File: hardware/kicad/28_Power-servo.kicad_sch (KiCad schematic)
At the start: 18 parts, among them U55 TPSM63610RDFR

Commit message: servo buck done
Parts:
- removed C67: 22pF, Capacitor_SMD:C_0402_1005Metric, symbol 5v rail sm-easyedapro:C0402C220K5RACAUTO
- removed JP2: Jumper_2_Bridged, Jumper:SolderJumper-2_P1.3mm_Bridged_RoundedPad1.0x1.5mm, symbol Jumper:Jumper_2_Bridged
- removed NT17: NetTie_2, NetTie:NetTie-2_SMD_Pad2.0mm, symbol Device:NetTie_2
- removed R118: 100kΩ, Resistor_SMD:R_0402_1005Metric, symbol 5v rail sm-easyedapro:FRC0402F1003TS
- added C1701: 100nF, Capacitor_SMD:C_0603_1608Metric, symbol Device:C
- added JP1701: Jumper_2_Small_Bridged, PCM_SparkFun-Jumper:Jumper_2_NC_Trace, symbol Jumper:Jumper_2_Small_Bridged
- added NT1702: NetTie_2, 5v rail sm-easyedapro:NetTie-2_SMD_Pad0.2mm, symbol Device:NetTie_2
- R117: footprint Resistor_SMD:R_0603_1608Metric -> Resistor_SMD:R_0402_1005Metric; LCSC Part Name 26.7kΩ ±1% 100mW 厚膜电阻 -> (none); Manufacturer UNI-ROYAL(厚声) -> (none); Manufacturer Part 0603WAF2672T5E -> (none); Supplier LCSC -> (none); Supplier Part C22923 -> (none)
- R120: footprint Resistor_SMD:R_0603_1608Metric -> Resistor_SMD:R_0402_1005Metric; LCSC Part Name 47kΩ ±1% 100mW 厚膜电阻 -> (none); Manufacturer UNI-ROYAL(厚声) -> (none); Manufacturer Part 0603WAF4702T5E -> (none); Supplier LCSC -> (none); Supplier Part C25819 -> (none)
- R121: now not fitted; now left out of the parts list
- R122: LCSC Part Name 100kΩ ±1% 62.5mW 厚膜电阻 -> (none); Manufacturer FOJAN(富捷) -> (none); Manufacturer Part FRC0402F1003TS -> (none); Supplier LCSC -> (none); Supplier Part C2906859 -> (none)
- R123: footprint Resistor_SMD:R_0603_1608Metric -> Resistor_SMD:R_0402_1005Metric; LCSC Part Name 20kΩ ±1% 100mW 厚膜电阻 -> (none); Manufacturer UNI-ROYAL(厚声) -> (none); Manufacturer Part 0603WAF2002T5E -> (none); Supplier LCSC -> (none); Supplier Part C4184 -> (none)
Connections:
- net GNDA: now also C65.1, C66.2, C68.2, C69.1, C70.1, C71.1, U55.19 (PGND), U55.20 (PGND), C1701.1, JP1701.2 (B), NT1702.1
- net OUT: now also C1701.2
- net at U55.14 (SPSP): now also JP1701.1 (A)
- net at U55.15 (MODE): now also NT1702.2
- removed net GND: C65.1, C66.2, C68.2, C69.1, C70.1, C71.1, U55.16 (NC), U55.19 (PGND), U55.20 (PGND)
- no-connect marks 2 -> 3
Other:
- note added: "highest efficiency, bad emi default cut trace an place 100 ohm for better balance"
- note removed: "highest efficiency, bad emi default cut trace for 100 ohm for better balance"

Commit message: starting erc check
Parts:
- C65, C66, C69, C70, C71: footprint Capacitor_SMD:C_1210_3225Metric -> 5v rail sm-easyedapro:C1210
- R117: footprint Resistor_SMD:R_0402_1005Metric -> 5v rail sm-easyedapro:R0603; LCSC Part Name (none) -> 26.7kΩ ±1% 100mW 厚膜电阻; Manufacturer (none) -> UNI-ROYAL(厚声); Manufacturer Part (none) -> 0603WAF2672T5E; Supplier (none) -> LCSC; Supplier Part (none) -> C22923
- R119: footprint Resistor_SMD:R_0402_1005Metric -> 5v rail sm-easyedapro:R0402
- R120: footprint Resistor_SMD:R_0402_1005Metric -> 5v rail sm-easyedapro:R0603; LCSC Part Name (none) -> 47kΩ ±1% 100mW 厚膜电阻; Manufacturer (none) -> UNI-ROYAL(厚声); Manufacturer Part (none) -> 0603WAF4702T5E; Supplier (none) -> LCSC; Supplier Part (none) -> C25819
- R121: footprint Resistor_SMD:R_0603_1608Metric -> 5v rail sm-easyedapro:R0603
- R122: footprint Resistor_SMD:R_0402_1005Metric -> 5v rail sm-easyedapro:R0402; LCSC Part Name (none) -> 100kΩ ±1% 62.5mW 厚膜电阻; Manufacturer (none) -> FOJAN(富捷); Manufacturer Part (none) -> FRC0402F1003TS; Supplier (none) -> LCSC; Supplier Part (none) -> C2906859
- R123: footprint Resistor_SMD:R_0402_1005Metric -> 5v rail sm-easyedapro:R0603; LCSC Part Name (none) -> 20kΩ ±1% 100mW 厚膜电阻; Manufacturer (none) -> UNI-ROYAL(厚声); Manufacturer Part (none) -> 0603WAF2002T5E; Supplier (none) -> LCSC; Supplier Part (none) -> C4184
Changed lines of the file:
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@@
 			)
 		)
-		(property "Footprint" "Capacitor_SMD:C_1210_3225Metric"
+		(property "Footprint" "5v rail sm-easyedapro:C1210"
 			(at 307.34 92.71 0)
 			(effects
@@
 			)
 		)
-		(property "Footprint" "Resistor_SMD:R_0402_1005Metric"
+		(property "Footprint" "5v rail sm-easyedapro:R0603"
 			(at 279.4 111.76 0)
 			(effects
@@
 			)
 		)
-		(property "Datasheet" ""
+		(property "Datasheet" "https://item.szlcsc.com/datasheet/0603WAF2002T5E/4591.html"
 			(at 279.4 111.76 0)
 			(effects
@@
 			)
 		)
-		(property "Description" ""
+		(property "Description" "Type:Thick Film Resistor Resistance:20kΩ Tolerance:±1% Tolerance:±1% Power(Watts):100mW Voltage-Supply(Max):75V Temperature Coefficient:±100ppm/°C Temperature Coefficient:±100ppm/°C Operating Temperature:-55°C~+155°C Operating Temperature:-55°C~+155°C"
 			(at 279.4 111.76 0)
 			(effects
@@
 			)
 		)
-		(property "Manufacturer Part" ""
+		(property "Manufacturer Part" "0603WAF2002T5E"
 			(at 279.4 111.76 0)
 			(effects
@@
 			)
 		)
-		(property "Manufacturer" ""
+		(property "Manufacturer" "UNI-ROYAL(厚声)"
 			(at 279.4 111.76 0)
 			(effects
@@
 			)
 		)
-		(property "Supplier Part" ""
+		(property "Supplier Part" "C4184"
 			(at 279.4 111.76 0)
 			(effects
@@
 			)
 		)
-		(property "Supplier" ""
+		(property "Supplier" "LCSC"
 			(at 279.4 111.76 0)
 			(effects
@@
 			)
 		)
-		(property "LCSC Part Name" ""
+		(property "LCSC Part Name" "20kΩ ±1% 100mW 厚膜电阻"
 			(at 279.4 111.76 0)
 			(effects
@@
 			)
 		)
-		(property "Footprint" "Capacitor_SMD:C_1210_3225Metric"
+		(property "Footprint" "5v rail sm-easyedapro:C1210"
 			(at 139.7 125.73 0)
 			(effects
@@
 			)
 		)
-		(property "Footprint" "Capacitor_SMD:C_1210_3225Metric"
+		(property "Footprint" "5v rail sm-easyedapro:C1210"
 			(at 334.01 92.71 0)
 			(effects
@@
 			)
 		)
-		(property "Datasheet" ""
+		(property "Datasheet" "~"
 			(at 220.98 107.95 0)
 			(effects
@@
 			)
 		)
-		(property "Description" ""
+		(property "Description" "Jumper, 2-pole, closed/bridged"
 			(at 220.98 107.95 0)
 			(effects
@@
 			)
 		)
-		(property "Description" ""
+		(property "Description" "Power symbol creates a global label with name \"GNDA\" , analog ground"
 			(at 243.84 144.78 0)
 			(effects
@@
 			)
 		)
-		(property "Footprint" "Capacitor_SMD:C_1210_3225Metric"
+		(property "Footprint" "5v rail sm-easyedapro:C1210"
 			(at 166.37 125.73 0)
 			(effects
@@
 			)
 		)
-		(property "Footprint" "Resistor_SMD:R_0402_1005Metric"
+		(property "Footprint" "5v rail sm-easyedapro:R0402"
 			(at 279.4 93.98 0)
 			(effects
@@
 			)
 		)
-		(property "Description" ""
+		(property "Description" "Type:Thick Film Resistor Resistance:100kΩ Tolerance:±1% Tolerance:±1% Power(Watts):62.5mW Voltage-Supply(Max):50V Temperature Coefficient:±100ppm/°C Temperature Coefficient:±100ppm/°C Operating Temperature:-55°C~+155°C Operating Temperature:-55°C~+155°C"
 			(at 279.4 93.98 0)
 			(effects
@@
 			)
 		)
-		(property "Manufacturer Part" ""
+		(property "Manufacturer Part" "FRC0402F1003TS"
 			(at 279.4 93.98 0)
 			(effects
@@
 			)
 		)
-		(property "Manufacturer" ""
+		(property "Manufacturer" "FOJAN(富捷)"
 			(at 279.4 93.98 0)
 			(effects
@@
 			)
 		)
-		(property "Supplier Part" ""
+		(property "Supplier Part" "C2906859"
 			(at 279.4 93.98 0)
 			(effects
@@
 			)
 		)
-		(property "Supplier" ""
+		(property "Supplier" "LCSC"
 			(at 279.4 93.98 0)
 			(effects
@@
 			)
 		)
-		(property "LCSC Part Name" ""
+		(property "LCSC Part Name" "100kΩ ±1% 62.5mW 厚膜电阻"
 			(at 279.4 93.98 0)
 			(effects
@@
 			)
 		)
-		(property "Description" ""
+		(property "Description" "Power symbol creates a global label with name \"GNDA\" , analog ground"
 			(at 44.45 132.08 0)
 			(effects
@@
 			)
 		)
-		(property "Description" ""
+		(property "Description" "Power symbol creates a global label with name \"GNDA\" , analog ground"
 			(at 279.4 137.16 0)
 			(effects
@@
 			)
 		)
-		(property "Footprint" "Resistor_SMD:R_0402_1005Metric"
+		(property "Footprint" "5v rail sm-easyedapro:R0603"
 			(at 36.83 119.38 0)
 			(effects
@@
 			)
 		)
-		(property "Datasheet" ""
+		(property "Datasheet" "https://item.szlcsc.com/datasheet/0603WAF2672T5E/23650.html"
 			(at 36.83 119.38 0)
 			(effects
@@
 			)
 		)
-		(property "Description" ""
+		(property "Description" "Type:Thick Film Resistor Resistance:26.7kΩ Tolerance:±1% Tolerance:±1% Power(Watts):100mW Voltage-Supply(Max):75V Temperature Coefficient:±100ppm/°C Temperature Coefficient:±100ppm/°C Operating Temperature:-55°C~+155°C Operating Temperature:-55°C~+155°C"
 			(at 36.83 119.38 0)
 			(effects
@@
 			)
 		)
-		(property "Manufacturer Part" ""
+		(property "Manufacturer Part" "0603WAF2672T5E"
 			(at 36.83 119.38 0)
 			(effects
@@
 			)
 		)
-		(property "Manufacturer" ""
+		(property "Manufacturer" "UNI-ROYAL(厚声)"
 			(at 36.83 119.38 0)
 			(effects
@@
 			)
 		)
-		(property "Supplier Part" ""
+		(property "Supplier Part" "C22923"
 			(at 36.83 119.38 0)
 			(effects
@@
 			)
 		)
-		(property "Supplier" ""
+		(property "Supplier" "LCSC"
 			(at 36.83 119.38 0)
 			(effects
@@
 			)
 		)
-		(property "LCSC Part Name" ""
+		(property "LCSC Part Name" "26.7kΩ ±1% 100mW 厚膜电阻"
 			(at 36.83 119.38 0)
 			(effects
@@
 			)
 		)
-		(property "Footprint" "Resistor_SMD:R_0402_1005Metric"
+		(property "Footprint" "5v rail sm-easyedapro:R0603"
 			(at 157.48 69.85 0)
 			(effects
@@
 			)
 		)
-		(property "Datasheet" ""
+		(property "Datasheet" "https://item.szlcsc.com/datasheet/0603WAF4702T5E/26562.html"
 			(at 157.48 69.85 0)
 			(effects
@@
 			)
 		)
-		(property "Description" ""
+		(property "Description" "Type:Thick Film Resistor Resistance:47kΩ Tolerance:±1% Tolerance:±1% Power(Watts):100mW Voltage-Supply(Max):75V Temperature Coefficient:±100ppm/°C Temperature Coefficient:±100ppm/°C Operating Temperature:-55°C~+155°C Operating Temperature:-55°C~+155°C"
 			(at 157.48 69.85 0)
 			(effects
@@
 			)
 		)
-		(property "Manufacturer Part" ""
+		(property "Manufacturer Part" "0603WAF4702T5E"
 			(at 157.48 69.85 0)
 			(effects
@@
 			)
 		)
-		(property "Manufacturer" ""
+		(property "Manufacturer" "UNI-ROYAL(厚声)"
 			(at 157.48 69.85 0)
 			(effects
@@
 			)
 		)
-		(property "Supplier Part" ""
+		(property "Supplier Part" "C25819"
 			(at 157.48 69.85 0)
 			(effects
@@
 			)
 		)
-		(property "Supplier" ""
+		(property "Supplier" "LCSC"
 			(at 157.48 69.85 0)
 			(effects
@@
 			)
 		)
-		(property "LCSC Part Name" ""
+		(property "LCSC Part Name" "47kΩ ±1% 100mW 厚膜电阻"
 			(at 157.48 69.85 0)
 			(effects
@@
 			)
 		)
-		(property "Description" ""
+		(property "Description" "Power symbol creates a global label with name \"GNDA\" , analog ground"
 			(at 115.57 127 0)
 			(effects
@@
 			)
 		)
-		(property "Footprint" "Resistor_SMD:R_0603_1608Metric"
+		(property "Footprint" "5v rail sm-easyedapro:R0603"
 			(at 234.95 107.95 0)
 			(effects
@@
 			)
 		)
-		(property "Footprint" "Capacitor_SMD:C_1210_3225Metric"
+		(property "Footprint" "5v rail sm-easyedapro:C1210"
 			(at 320.04 92.71 0)
 			(effects
@@
 			)
 		)
-		(property "Description" ""
+		(property "Description" "Power symbol creates a global label with name \"GNDA\" , analog ground"
 			(at 201.93 138.43 0)
 			(effects
@@
 			)
 		)
-		(property "Footprint" "Resistor_SMD:R_0402_1005Metric"
+		(property "Footprint" "5v rail sm-easyedapro:R0402"
 			(at 115.57 110.49 0)
 			(effects
@@
 			)
 		)
-		(property "Description" "Power-5V"
+		(property "Description" "Power symbol creates a global label with name \"+3V3\""
 			(at 157.48 63.5 0)
 			(effects
@@
 			)
 		)
-		(property "Description" ""
+		(property "Description" "Power symbol creates a global label with name \"GNDA\" , analog ground"
 			(at 92.71 128.27 0)
 			(effects

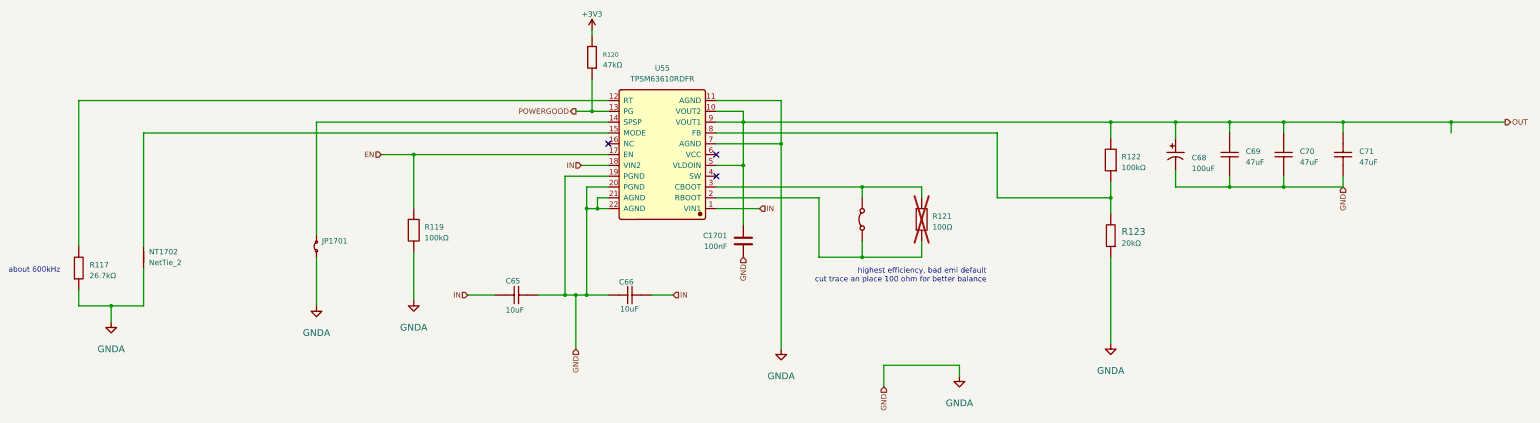
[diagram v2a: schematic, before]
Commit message: fixed some drc issues
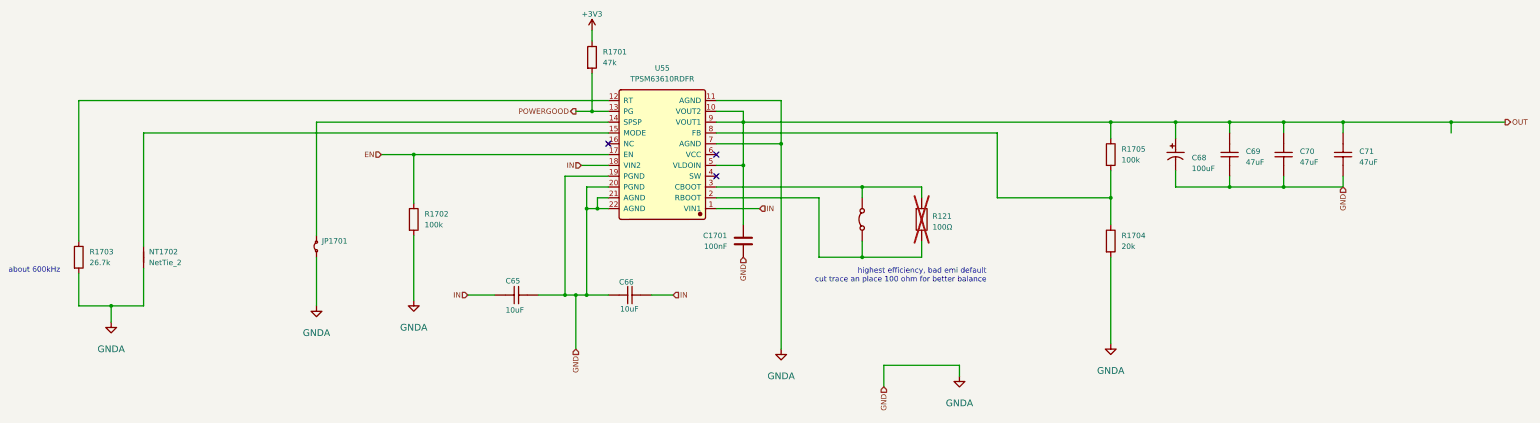
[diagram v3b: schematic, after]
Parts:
- removed R117: 26.7kΩ, 5v rail sm-easyedapro:R0603, symbol 5v rail sm-easyedapro:0603WAF2672T5E
- removed R119, R122: 100kΩ, 5v rail sm-easyedapro:R0402, symbol 5v rail sm-easyedapro:FRC0402F1003TS
- removed R120: 47kΩ, 5v rail sm-easyedapro:R0603, symbol 5v rail sm-easyedapro:0603WAF4702T5E
- removed R123: 20kΩ, 5v rail sm-easyedapro:R0603, symbol 5v rail sm-easyedapro:0603WAF2002T5E
- added R1701: 47k, Resistor_SMD:R_0402_1005Metric, symbol Device:R
- added R1702, R1705: 100k, Resistor_SMD:R_0402_1005Metric, symbol Device:R
- added R1703: 26.7k, Resistor_SMD:R_0402_1005Metric, symbol Device:R
- added R1704: 20k, Resistor_SMD:R_0402_1005Metric, symbol Device:R
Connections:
- net +3V3: now also R1701.1
- net EN: now also R1702.1
- net GNDA: now also R1702.2, R1703.2, R1704.2
- net OUT: now also R1705.1
- net POWERGOOD: now also R1701.2
- net at U55.8 (FB): now also R1704.1, R1705.2
- net at U55.12 (RT): now also R1703.1

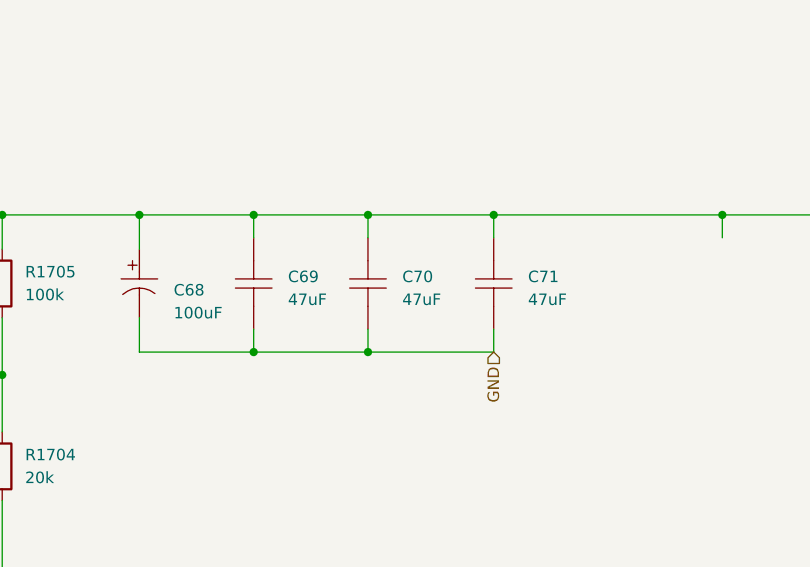
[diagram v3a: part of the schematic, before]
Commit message: about to switch to 3v3 reg instead of buck
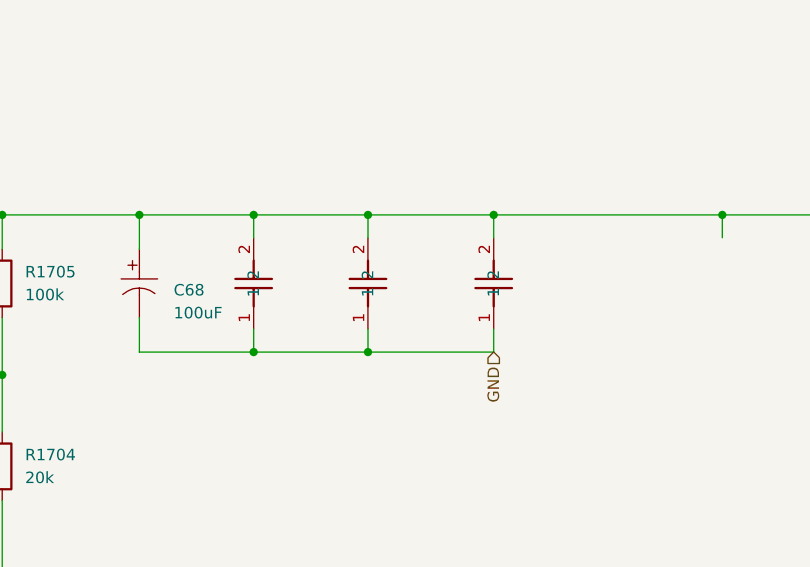
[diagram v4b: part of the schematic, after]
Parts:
- removed C69, C70, C71: 47uF, 5v rail sm-easyedapro:C1210, symbol 5v rail sm-easyedapro:CS3225X7R476K160NRL
- added C1702, C1703, C1704: GRM32ER71A476ME15L, JLCImport:GRM32ER71A476ME15L, symbol JLCImport:GRM32ER71A476ME15L
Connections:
- net GNDA: now also C1702.1, C1703.1, C1704.1
- net OUT: now also C1702.2, C1703.2, C1704.2

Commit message: updating symbols to use kicad footprints where possible
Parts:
- C65, C66: footprint 5v rail sm-easyedapro:C1210 -> Capacitor_SMD:C_1210_3225Metric
- R121: footprint 5v rail sm-easyedapro:R0603 -> Resistor_SMD:R_0603_1608Metric
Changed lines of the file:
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@@
 			)
 		)
-		(property "Footprint" "5v rail sm-easyedapro:C1210"
+		(property "Footprint" "Capacitor_SMD:C_1210_3225Metric"
 			(at 139.7 125.73 0)
 			(effects
@@
 			)
 		)
-		(property "Footprint" "5v rail sm-easyedapro:C1210"
+		(property "Footprint" "Capacitor_SMD:C_1210_3225Metric"
 			(at 166.37 125.73 0)
 			(effects
@@
 			)
 		)
-		(property "Footprint" "5v rail sm-easyedapro:R0603"
+		(property "Footprint" "Resistor_SMD:R_0603_1608Metric"
 			(at 234.95 107.95 0)
 			(effects

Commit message: switched some more
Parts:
- C1702, C1703, C1704: footprint JLCImport:GRM32ER71A476ME15L -> Capacitor_SMD:C_1210_3225Metric
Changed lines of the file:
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@@
 			)
 		)
-		(property "Footprint" "JLCImport:GRM32ER71A476ME15L"
+		(property "Footprint" "Capacitor_SMD:C_1210_3225Metric"
 			(at 334.01 92.71 0)
 			(effects
@@
 			)
 		)
-		(property "Footprint" "JLCImport:GRM32ER71A476ME15L"
+		(property "Footprint" "Capacitor_SMD:C_1210_3225Metric"
 			(at 320.04 92.71 0)
 			(effects
@@
 			)
 		)
-		(property "Footprint" "JLCImport:GRM32ER71A476ME15L"
+		(property "Footprint" "Capacitor_SMD:C_1210_3225Metric"
 			(at 307.34 92.71 0)
 			(effects

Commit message: updates
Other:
- note added: "MAX 6V"
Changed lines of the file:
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@@
+		)
+	)
+	(text "MAX 6V"
+		(exclude_from_sim no)
+		(at 312.166 80.772 0)
+		(effects
+			(font
+				(size 1.27 1.27)
+			)
 		)
 	)
